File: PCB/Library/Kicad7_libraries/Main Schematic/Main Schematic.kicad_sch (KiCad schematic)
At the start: 0 parts

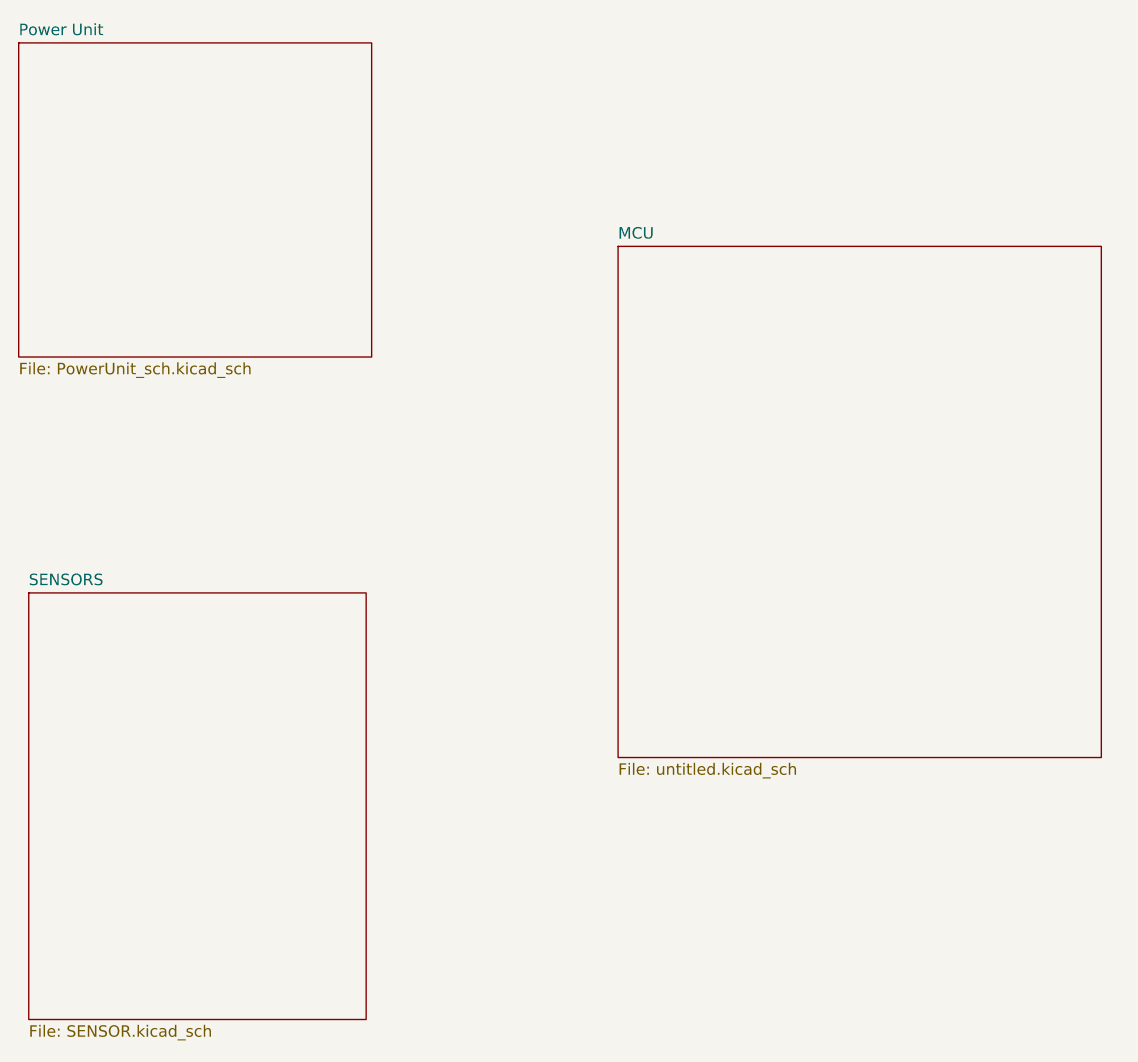
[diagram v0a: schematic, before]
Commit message: I recreated our schematics into hierachy sheets instead of individual sheets
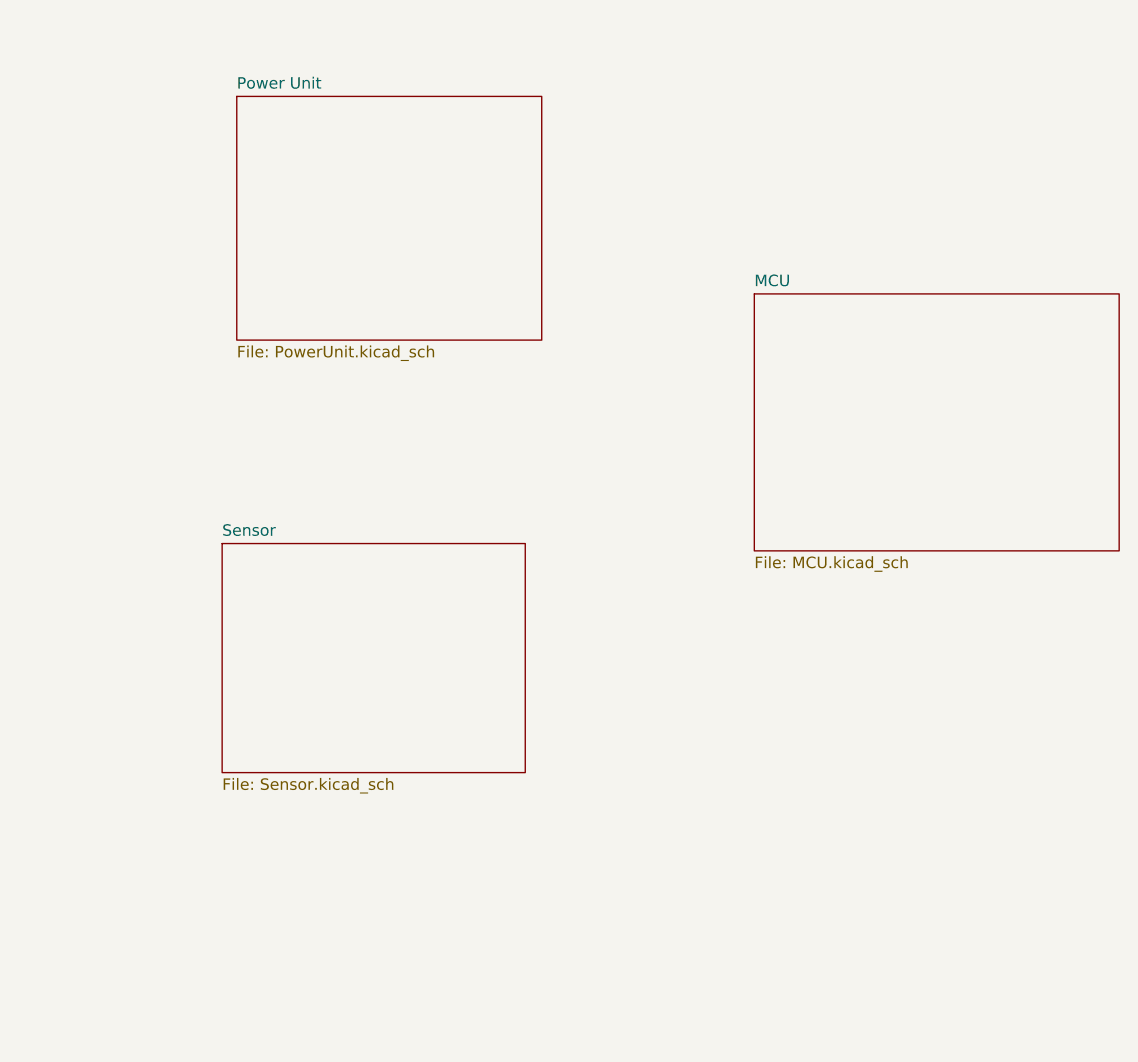
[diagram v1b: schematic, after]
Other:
- removed sheet SENSORS
- added sheet Sensor (Sensor.kicad_sch)
- sheet MCU: file untitled.kicad_sch -> MCU.kicad_sch
- sheet Power Unit: file PowerUnit_sch.kicad_sch -> PowerUnit.kicad_sch
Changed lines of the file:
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@@
 (kicad_sch (version 20230121) (generator eeschema)
   (paper "A4")
-  (sheet (at 50.7492 122.2756) (size 37.4904 47.3964) (fields_autoplaced)
+  (sheet (at 131.3688 89.0524) (size 40.5384 28.5496) (fields_autoplaced)
     (stroke (width 0.1524) (type solid))
     (fill (color 0 0 0 0.0000))
-    (property "Sheetname" "SENSORS" (at 50.7492 121.564 0)
+    (property "Sheetname" "MCU" (at 131.3688 88.3408 0)
       (effects (font (size 1.27 1.27)) (justify left bottom))
     )
-    (property "Sheetfile" "SENSOR.kicad_sch" (at 50.7492 170.2566 0)
+    (property "Sheetfile" "MCU.kicad_sch" (at 131.3688 118.1866 0)
       (effects (font (size 1.27 1.27)) (justify left top))
     )
     (instances
       (project "Main Schematic"
-        (path "/7e8c9ffe-1b32-4326-ae61-8877b5395b8a" (page "4"))
+        (path "/81c41bad-bb43-41af-b405-18d135a809b1" (page "2"))
       )
     )
   )
-  (sheet (at 49.6316 61.1632) (size 39.2176 34.8996) (fields_autoplaced)
+  (sheet (at 72.2376 116.7892) (size 33.6804 25.4508) (fields_autoplaced)
     (stroke (width 0.1524) (type solid))
     (fill (color 0 0 0 0.0000))
-    (property "Sheetname" "Power Unit" (at 49.6316 60.4516 0)
+    (property "Sheetname" "Sensor" (at 72.2376 116.0776 0)
       (effects (font (size 1.27 1.27)) (justify left bottom))
     )
-    (property "Sheetfile" "PowerUnit_sch.kicad_sch" (at 49.6316 96.6474 0)
+    (property "Sheetfile" "Sensor.kicad_sch" (at 72.2376 142.8246 0)
       (effects (font (size 1.27 1.27)) (justify left top))
     )
     (instances
       (project "Main Schematic"
-        (path "/7e8c9ffe-1b32-4326-ae61-8877b5395b8a" (page "3"))
+        (path "/81c41bad-bb43-41af-b405-18d135a809b1" (page "4"))
       )
     )
   )
-  (sheet (at 116.2304 83.7692) (size 53.6956 56.7944) (fields_autoplaced)
+  (sheet (at 73.8632 67.1068) (size 33.8836 27.0764) (fields_autoplaced)
     (stroke (width 0.1524) (type solid))
     (fill (color 0 0 0 0.0000))
-    (property "Sheetname" "MCU" (at 116.2304 83.0576 0)
+    (property "Sheetname" "Power Unit" (at 73.8632 66.3952 0)
       (effects (font (size 1.27 1.27)) (justify left bottom))
     )
-    (property "Sheetfile" "untitled.kicad_sch" (at 116.2304 141.1482 0)
+    (property "Sheetfile" "PowerUnit.kicad_sch" (at 73.8632 94.7678 0)
       (effects (font (size 1.27 1.27)) (justify left top))
     )
     (instances
       (project "Main Schematic"
-        (path "/7e8c9ffe-1b32-4326-ae61-8877b5395b8a" (page "2"))
+        (path "/81c41bad-bb43-41af-b405-18d135a809b1" (page "3"))
       )
     )

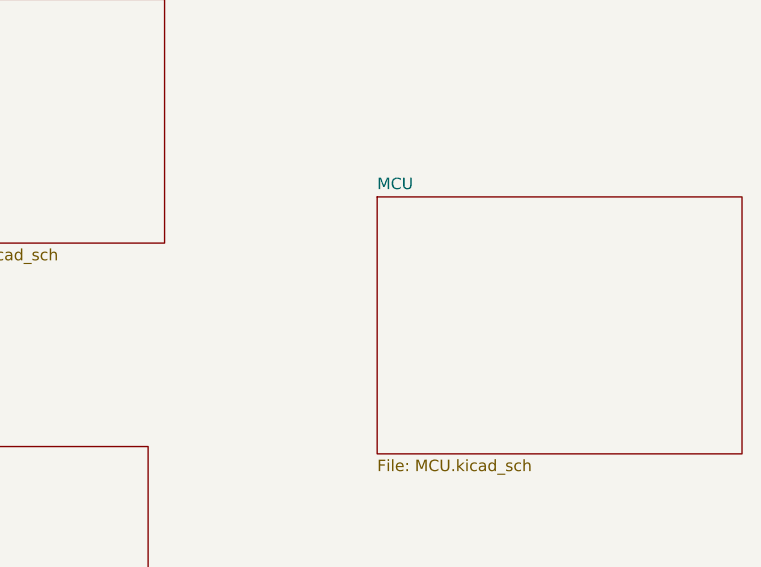
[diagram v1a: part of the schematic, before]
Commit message: Updated the MCU
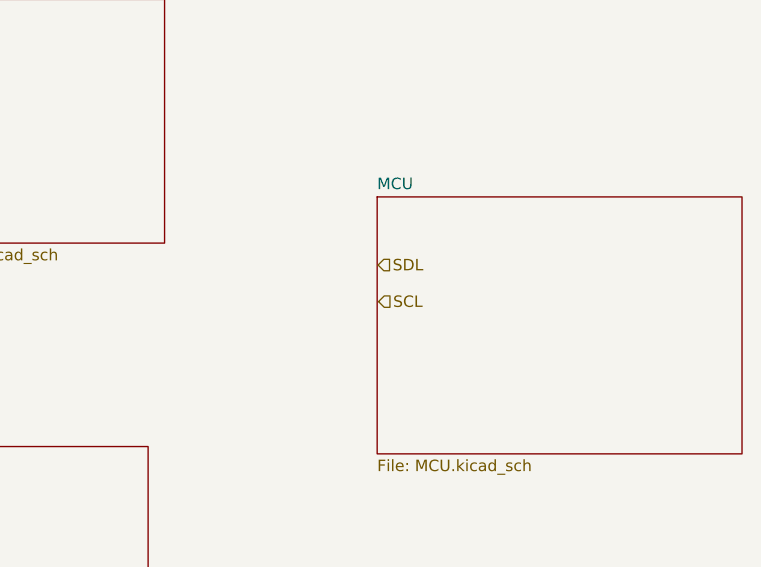
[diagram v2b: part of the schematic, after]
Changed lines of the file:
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@@
 (kicad_sch (version 20230121) (generator eeschema)
   (paper "A4")
+  (hierarchical_label "SCL" (shape input) (at 131.5212 100.6856 0) (fields_autoplaced)
+    (effects (font (size 1.27 1.27)) (justify left))
+  )
+  (hierarchical_label "SDL" (shape input) (at 131.4704 96.6216 0) (fields_autoplaced)
+    (effects (font (size 1.27 1.27)) (justify left))
+  )
   (sheet (at 131.3688 89.0524) (size 40.5384 28.5496) (fields_autoplaced)
     (stroke (width 0.1524) (type solid))

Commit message: updated sche
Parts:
- added J2: USB_B_Micro, symbol Connector:USB_B_Micro
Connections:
- new net GND: J2.4 (ID), J2.5 (GND), J2.6 (Shield)
- new net USB D+: J2.3 (D+)
- new net USB D-: J2.2 (D-)
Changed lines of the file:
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@@
 (kicad_sch (version 20230121) (generator eeschema)
   (paper "A4")
+  (junction (at 142.24 58.42) (diameter 0) (color 0 0 0 0)
+  )
+  (junction (at 140.97 58.42) (diameter 0) (color 0 0 0 0)
+  )
+  (wire (pts (xy 149.86 44.45) (xy 154.94 44.45))
+    (stroke (width 0) (type default))
+  )
+  (wire (pts (xy 153.67 58.42) (xy 142.24 58.42))
+    (stroke (width 0) (type default))
+  )
+  (wire (pts (xy 149.86 49.53) (xy 153.67 49.53))
+    (stroke (width 0) (type default))
+  )
+  (wire (pts (xy 153.67 49.53) (xy 153.67 58.42))
+    (stroke (width 0) (type default))
+  )
+  (wire (pts (xy 149.86 46.99) (xy 154.94 46.99))
+    (stroke (width 0) (type default))
+  )
+  (polyline (pts (xy 168.91 71.12) (xy 281.94 71.12))
+    (stroke (width 0) (type default))
+  )
+  (wire (pts (xy 140.97 60.96) (xy 140.97 58.42))
+    (stroke (width 0) (type default))
+  )
+  (wire (pts (xy 140.97 58.42) (xy 142.24 58.42))
+    (stroke (width 0) (type default))
+  )
+  (wire (pts (xy 140.97 58.42) (xy 139.7 58.42))
+    (stroke (width 0) (type default))
+  )
+  (wire (pts (xy 142.24 58.42) (xy 142.24 54.61))
+    (stroke (width 0) (type default))
+  )
+  (wire (pts (xy 139.7 58.42) (xy 139.7 54.61))
+    (stroke (width 0) (type default))
+  )
+  (global_label "USB D+" (shape input) (at 154.94 44.45 0) (fields_autoplaced)
+    (effects (font (size 1.27 1.27)) (justify left))
+    (property "Intersheetrefs" "${INTERSHEET_REFS}" (at 165.2602 44.45 0)
+      (effects (font (size 1.27 1.27)) (justify left) hide)
+    )
+  )
+  (global_label "USB D-" (shape input) (at 154.94 46.99 0) (fields_autoplaced)
+    (effects (font (size 1.27 1.27)) (justify left))
+    (property "Intersheetrefs" "${INTERSHEET_REFS}" (at 165.2602 46.99 0)
+      (effects (font (size 1.27 1.27)) (justify left) hide)
+    )
+  )
   (hierarchical_label "SCL" (shape input) (at 131.5212 100.6856 0) (fields_autoplaced)
     (effects (font (size 1.27 1.27)) (justify left))
@@
     (effects (font (size 1.27 1.27)) (justify left))
   )
+  (symbol (lib_id "Connector:USB_B_Micro") (at 142.24 44.45 0) (unit 1)
+    (in_bom yes) (on_board yes) (dnp no)
+    (property "Reference" "J2" (at 143.6878 32.5882 0)
+      (effects (font (size 1.27 1.27)))
+    )
+    (property "Value" "USB_B_Micro" (at 143.6878 34.8996 0)
+      (effects (font (size 1.27 1.27)))
+    )
+    (property "Footprint" "" (at 146.05 45.72 0)
+      (effects (font (size 1.27 1.27)) hide)
+    )
+    (property "Datasheet" "~" (at 146.05 45.72 0)
+      (effects (font (size 1.27 1.27)) hide)
+    )
+    (pin "1")
+    (pin "2")
+    (pin "3")
+    (pin "4")
+    (pin "5")
+    (pin "6")
+    (instances
+      (project "Main Schematic"
+        (path "/7e8c9ffe-1b32-4326-ae61-8877b5395b8a/98e117a5-3aeb-416f-98c5-160b7cf15fec"
+          (reference "J2") (unit 1)
+        )
+      )
+      (project "Main Schematic"
+        (path "/81c41bad-bb43-41af-b405-18d135a809b1/be77d6c5-6f74-462b-ad7c-0ffad190e576"
+          (reference "J2") (unit 1)
+        )
+        (path "/81c41bad-bb43-41af-b405-18d135a809b1"
+          (reference "J3") (unit 1)
+        )
+      )
+      (project "PowerUnit_sch"
+        (path "/94a75581-cd2d-4b84-bb57-dd404d2f6711"
+          (reference "J2") (unit 1)
+        )
+      )
+      (project "power supplly[2803]"
+        (path "/ef6f5e70-2168-4df2-b1ca-c7d9a0d51980"
+          (reference "J2") (unit 1)
+        )
+      )
+    )
+  )
+  (symbol (lib_id "power:GND") (at 140.97 60.96 0) (unit 1)
+    (in_bom yes) (on_board yes) (dnp no)
+    (property "Reference" "#PWR015" (at 140.97 67.31 0)
+      (effects (font (size 1.27 1.27)) hide)
+    )
+    (property "Value" "GND" (at 141.097 65.3542 0)
+      (effects (font (size 1.27 1.27)))
+    )
+    (property "Footprint" "" (at 140.97 60.96 0)
+      (effects (font (size 1.27 1.27)) hide)
+    )
+    (property "Datasheet" "" (at 140.97 60.96 0)
+      (effects (font (size 1.27 1.27)) hide)
+    )
+    (pin "1")
+    (instances
+      (project "Main Schematic"
+        (path "/7e8c9ffe-1b32-4326-ae61-8877b5395b8a/98e117a5-3aeb-416f-98c5-160b7cf15fec"
+          (reference "#PWR015") (unit 1)
+        )
+      )
+      (project "Main Schematic"
+        (path "/81c41bad-bb43-41af-b405-18d135a809b1/be77d6c5-6f74-462b-ad7c-0ffad190e576"
+          (reference "#PWR013") (unit 1)
+        )
+        (path "/81c41bad-bb43-41af-b405-18d135a809b1"
+          (reference "#PWR012") (unit 1)
+        )
+      )
+      (project "PowerUnit_sch"
+        (path "/94a75581-cd2d-4b84-bb57-dd404d2f6711"
+          (reference "#PWR015") (unit 1)
+        )
+      )
+      (project "power supplly[2803]"
+        (path "/ef6f5e70-2168-4df2-b1ca-c7d9a0d51980"
+          (reference "#PWR0105") (unit 1)
+        )
+      )
+    )
+  )
   (sheet (at 131.3688 89.0524) (size 40.5384 28.5496) (fields_autoplaced)
